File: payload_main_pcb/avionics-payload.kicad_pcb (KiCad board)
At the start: 2 copper layers, 80 x 80 mm, 27 parts, among them J1 Micro_SD_Card, J2 Conn_Coaxial_x2, J3 Screw_Terminal_01x02, SW1 SW_Push, SW2 SW_Push, SW3 SW_Push, U2 Teensy4.0, U3 RFM96W-433S2, U4 LT1129-3.3_SOT223, U5 ublox_SAM-M8Q, U6 MS5607-02BA, U7 ADIS16470AMLZ

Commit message: Lots of stuff
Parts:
- removed the J2 at (44.5, 44.5)
- removed the R1 at (51.0, 84.4)
- removed the Ref** at (69.8, 75.6)
- added C2: 100nF, Capacitor_SMD:C_1206_3216Metric_Pad1.42x1.75mm_HandSolder, F.Cu at (52.7, 63.5)
- added C5: 100nF, Capacitor_SMD:C_1206_3216Metric_Pad1.42x1.75mm_HandSolder, F.Cu at (103.5, 95.2)
- added C6: 100nF, Capacitor_SMD:C_1206_3216Metric_Pad1.42x1.75mm_HandSolder, F.Cu at (87.0, 43.0)
- added J1: USB_C_Receptacle_USB2.0, Connector_USB:USB_C_Receptacle_GCT_USB4085, F.Cu at (76.8, 49.5)
- added J3: Conn_Coaxial, Connector_Coaxial:SMA_Amphenol_132291_Vertical, F.Cu at (63.2, 45.0)
- added R10: 51, Resistor_SMD:R_1206_3216Metric_Pad1.42x1.75mm_HandSolder, F.Cu at (101.4, 72.4)
- added R11: 10, Resistor_SMD:R_1206_3216Metric_Pad1.42x1.75mm_HandSolder, F.Cu at (101.4, 69.7)
- added R5: 51, Resistor_SMD:R_1206_3216Metric_Pad1.42x1.75mm_HandSolder, F.Cu at (101.3, 61.0)
- added R6: 10, Resistor_SMD:R_1206_3216Metric_Pad1.42x1.75mm_HandSolder, F.Cu at (101.3, 58.3)
- added R8: 51, Resistor_SMD:R_1206_3216Metric_Pad1.42x1.75mm_HandSolder, F.Cu at (101.3, 66.5)
- added R9: 10, Resistor_SMD:R_1206_3216Metric_Pad1.42x1.75mm_HandSolder, F.Cu at (101.3, 64.0)
- added REF**: MountingHole_3.2mm_M3_Pad_Via, MountingHole:MountingHole_3.2mm_M3_Pad_Via, F.Cu at (54.6, 44.5)
- added REF**: MountingHole_3.2mm_M3_Pad_Via, MountingHole:MountingHole_3.2mm_M3_Pad_Via, F.Cu at (54.6, 115.6)
- added REF**: MountingHole_3.2mm_M3_Pad_Via, MountingHole:MountingHole_3.2mm_M3_Pad_Via, F.Cu at (115.6, 44.5)
- added REF**: MountingHole_3.2mm_M3_Pad_Via, MountingHole:MountingHole_3.2mm_M3_Pad_Via, F.Cu at (115.6, 115.6)
- added Ref**: Val**, footprints:logo, F.Cu at (36.3, 114.3)
- added U3: 74LS14, Package_DIP:DIP-14_W7.62mm_SMDSocket_SmallPads, F.Cu at (97.8, 45.7)
- D1, D2, D3, D4: value LED -> LED_RGBA; footprint LED_SMD:LED_1206_3216Metric_Pad1.42x1.75mm_HandSolder -> LED_SMD:LED_Avago_PLCC4_3.2x2.8mm_CW
- R2: value 220 -> R; footprint Resistor_SMD:R_0805_2012Metric_Pad1.15x1.40mm_HandSolder -> Resistor_SMD:R_1206_3216Metric_Pad1.42x1.75mm_HandSolder
- R3: value 220 -> 51; footprint Resistor_SMD:R_0805_2012Metric_Pad1.15x1.40mm_HandSolder -> Resistor_SMD:R_1206_3216Metric_Pad1.42x1.75mm_HandSolder
- R4: value 220 -> 10; footprint Resistor_SMD:R_0805_2012Metric_Pad1.15x1.40mm_HandSolder -> Resistor_SMD:R_1206_3216Metric_Pad1.42x1.75mm_HandSolder
- moved C4 79.5 mm to (67.1, 115.6), turned to 0 degrees
- moved J4 76.6 mm to (99.1, 116.2)
- moved D1 75.9 mm to (116.2, 53.2)
- moved D2 75.0 mm to (116.2, 59.1)
- moved U6 72.9 mm to (67.9, 112.4), turned to 90 degrees
- moved D4 72.8 mm to (116.3, 70.5)
- moved R3 66.8 mm to (101.3, 55.1), turned to 180 degrees
- moved D3 66.6 mm to (116.2, 64.8)
- moved R4 61.2 mm to (101.3, 52.5), turned to 180 degrees
- moved C3 56.3 mm to (106.7, 114.9), turned to 0 degrees
- moved R12 51.6 mm to (75.2, 113.8), turned to 90 degrees
- moved SW1 50.8 mm to (59.7, 106.7), turned to 180 degrees
- moved R7 49.4 mm to (75.6, 58.4), turned to 90 degrees
- moved R1 47.7 mm to (74.9, 101.4), turned to 270 degrees
- moved J2 47.4 mm to (87.0, 65.2), turned to 0 degrees
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- renumbered C10 to C3, C9 to C4, J1 to J2, J3 to J4, R5 to R1, R7 to R12, R6 to R7, SW3 to SW1, SW1 to SW2, SW2 to SW3, U7 to U1, U3 to U4, U4 to U5, U5 to U7
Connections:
- D1 pad 2: SystemStatus -> Net-(D1-Pad2)
- D2 pad 2: SensorStatus -> Net-(D2-Pad2)
- D3 pad 2: TransmitterStatus -> Net-(D3-Pad2)
- D4 pad 2: GPSStatus -> Net-(D4-Pad2)
- R2 pad 1: GND -> +3V3
- R2 pad 2: Net-(D2-Pad1) -> Net-(J1-PadA5)
- R3 pad 1: GND -> Net-(D1-Pad1)
- R3 pad 2: Net-(D3-Pad1) -> SystemStatus
- R4 pad 1: GND -> Net-(D1-Pad2)
- R4 pad 2: Net-(D4-Pad1) -> Net-(R4-Pad2)
- U2 pad 10: TX1 -> IMU_DR
- U2 pad 23: Net-(U2-Pad23) -> RX1
- U2 pad 24: Net-(U2-Pad24) -> TX1
- U2 pad 27: Net-(U2-Pad27) -> GPSStatus
- U2 pad 28: IMU_DR -> TransmitterStatus
- U2 pad 29: Net-(U2-Pad29) -> SensorStatus
- U2 pad 30: Net-(U2-Pad30) -> SystemStatus
- U2 pad 34: Net-(U2-Pad34) -> V_USB
- U2 pad 4: GPSStatus -> Net-(U2-Pad4)
- U2 pad 5: SensorStatus -> Net-(U2-Pad5)
- U2 pad 53: Net-(U2-Pad53) -> USB_D-
- U2 pad 54: Net-(U2-Pad54) -> USB_D+
- U2 pad 6: TransmitterStatus -> Net-(U2-Pad6)
- U2 pad 7: SystemStatus -> Net-(U2-Pad7)
- U2 pad 9: RX1 -> Net-(U2-Pad9)
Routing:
- net GND: track 408.1 -> 0.00 mm, vias 2 -> 0
- net +3V3: track 202.1 -> 251.5 mm, vias 0 -> 6
- net V_USB: track 0.00 -> 47.8 mm, vias 0 -> 1
- net USB_D-: track 0.00 -> 37.2 mm, vias 0 -> 1
- net USB_D+: track 0.00 -> 35.8 mm, vias 0 -> 1
- net MOSI2: track 17.8 -> 51.1 mm, vias 0 -> 1
- net MISO2: track 46.8 -> 18.0 mm
- net SCK2: track 23.9 -> 51.7 mm, vias 0 -> 1
- net CS2: track 56.8 -> 29.9 mm, vias 1 -> 0
- net Net-(J1-PadA5): track 0.00 -> 25.9 mm
- net Net-(R11-Pad2): track 0.00 -> 24.0 mm, vias 0 -> 2
- net Net-(R6-Pad2): track 0.00 -> 20.3 mm, vias 0 -> 2
- net Net-(D1-Pad1): track 32.3 -> 13.0 mm
- net Net-(R9-Pad2): track 0.00 -> 16.7 mm, vias 0 -> 2
- net Net-(SW1-Pad2): track 0.00 -> 16.4 mm
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- added copper zone on F.Cu, net GND
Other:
- board size 80 x 80 mm -> 69.8 x 80 mm
- board text added: "Designed for SOAR's Asterion"
- board text added: "GPS"
- board text added: "GPS Reset"
- board text added: "IMU Reset"
- board text added: "Sensors"
- board text added: "System"
- board text added: "Transmitter"
- board text added: "Transmitter Reset"
- board text removed: "GPS Status"
- board text removed: "Sensors Status"
- board text removed: "System Status"
- board text removed: "Transmitter Status"

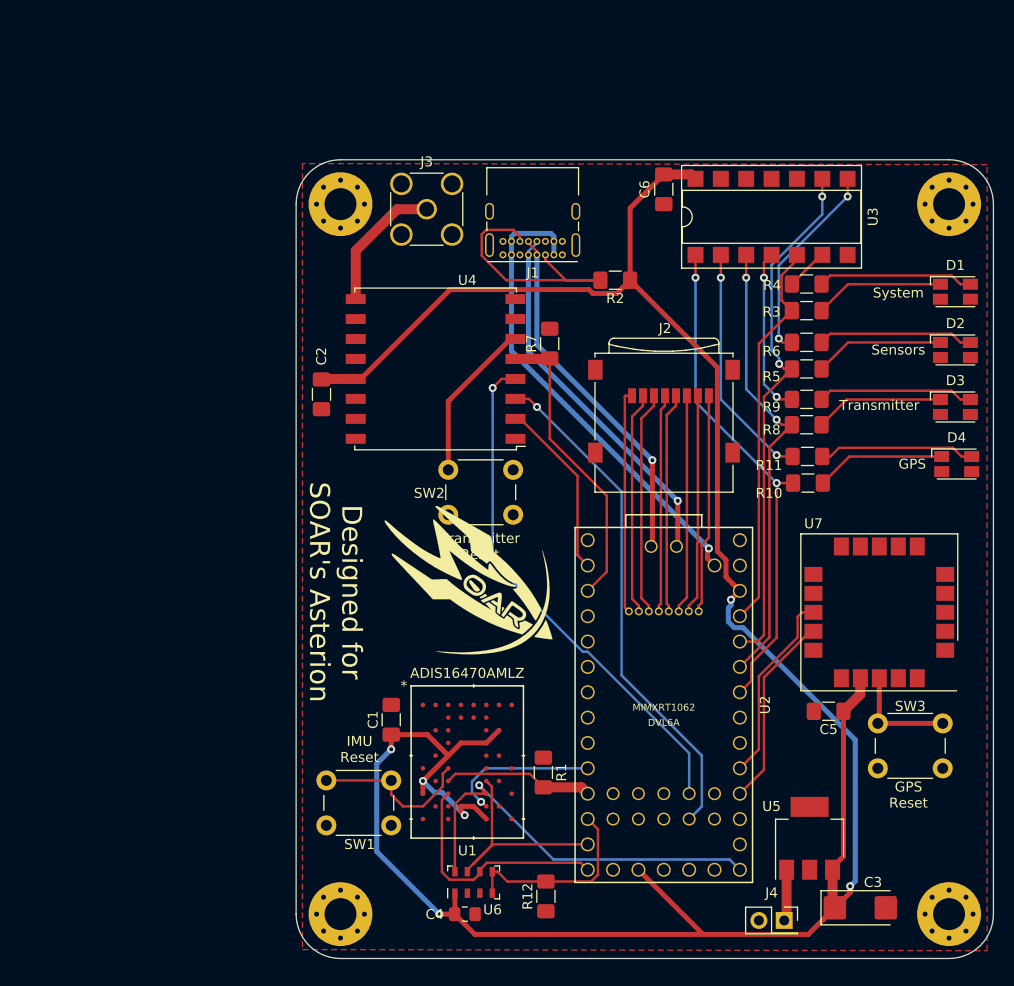
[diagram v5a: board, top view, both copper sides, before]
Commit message: Changed buttons and added bottom plane
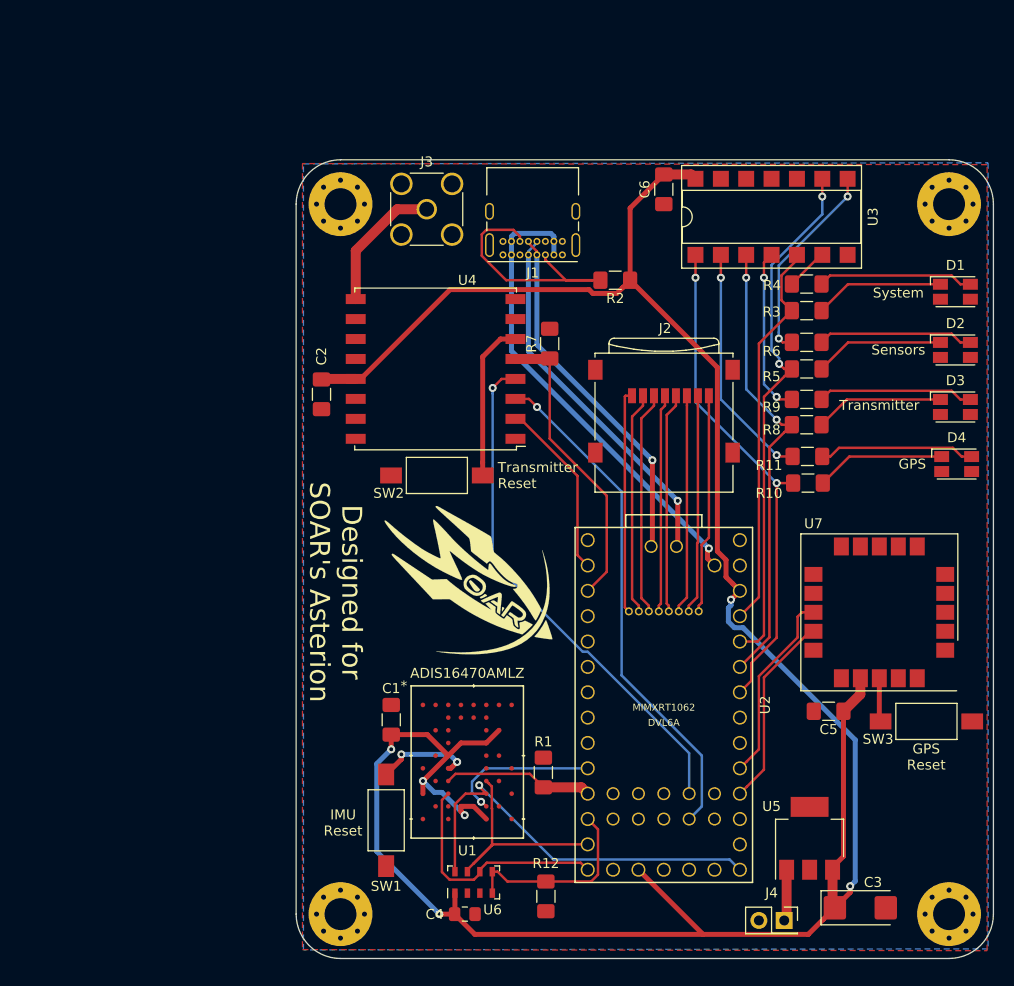
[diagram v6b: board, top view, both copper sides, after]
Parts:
- SW1, SW2, SW3: footprint Button_Switch_THT:SW_PUSH_6mm -> Button_Switch_SMD:SW_SPST_FSMSM
- moved SW2 8.60 mm to (64.3, 71.6), turned to 0 degrees
- moved SW3 4.97 mm to (113.3, 96.3)
- moved SW1 0.72 mm to (59.2, 106.2), turned to 90 degrees
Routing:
- net Net-(SW1-Pad2): track 16.4 -> 9.70 mm, vias 0 -> 2
- net Net-(SW3-Pad2): track 11.1 -> 4.38 mm
- added copper zone on B.Cu, net GND

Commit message: PCB REV A
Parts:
- removed the REF** at (54.6, 44.5)
- removed the REF** at (54.6, 115.6)
- removed the REF** at (115.6, 44.5)
- removed the REF** at (115.6, 115.6)
- added BT1: Battery_Cell, Battery:BatteryHolder_Keystone_1060_1x2032, B.Cu at (48.5, 69.3)
- added BZ1: Buzzer, Buzzer_Beeper:Buzzer_CUI_CPT-9019S-SMT, F.Cu at (70.5, 40.0)
- added C7: 100nF, Capacitor_SMD:C_1206_3216Metric_Pad1.42x1.75mm_HandSolder, F.Cu at (107.2, 78.7)
- added C8: 100nF, Capacitor_SMD:C_1206_3216Metric_Pad1.42x1.75mm_HandSolder, F.Cu at (107.2, 73.5)
- added C9: 100nF, Capacitor_SMD:C_1206_3216Metric_Pad1.42x1.75mm_HandSolder, F.Cu at (59.7, 70.8)
- added F1: Polyfuse, Fuse:Fuse_1812_4532Metric_Pad1.30x3.40mm_HandSolder, F.Cu at (82.5, 105.0)
- added J5: Conn_01x08, Connector_PinSocket_2.54mm:PinSocket_1x08_P2.54mm_Vertical, F.Cu at (41.0, 97.8)
- added R13: 11k, Resistor_SMD:R_1206_3216Metric_Pad1.42x1.75mm_HandSolder, F.Cu at (93.6, 91.8)
- added R14: 10M, Resistor_SMD:R_1206_3216Metric_Pad1.42x1.75mm_HandSolder, F.Cu at (61.0, 79.3)
- added R15: 3.3M, Resistor_SMD:R_1206_3216Metric_Pad1.42x1.75mm_HandSolder, F.Cu at (59.7, 74.8)
- added REF**: MountingHole_3.2mm_M3_Pad, MountingHole:MountingHole_3.2mm_M3_Pad, F.Cu at (104.0, 47.0)
- added REF**: MountingHole_3.2mm_M3_Pad, MountingHole:MountingHole_3.2mm_M3_Pad, F.Cu at (104.0, 93.0)
- added REF**: MountingHole_3.2mm_M3_Pad, MountingHole:MountingHole_3.2mm_M3_Pad, F.Cu at (36.0, 93.0)
- added REF**: MountingHole_3.2mm_M3_Pad, MountingHole:MountingHole_3.2mm_M3_Pad, F.Cu at (36.0, 47.0)
- added SW4: SW_SPST, Button_Switch_SMD:SW_DIP_SPSTx01_Slide_6.7x4.1mm_W6.73mm_P2.54mm_LowProfile_JPin, F.Cu at (74.1, 104.9)
- added TP1: TestPoint, Connector_Pin:Pin_D1.0mm_L10.0mm, F.Cu at (103.1, 68.7)
- added TP2: TestPoint, TestPoint:TestPoint_Loop_D2.50mm_Drill1.0mm, F.Cu at (58.5, 64.0)
- added TP3: TestPoint, TestPoint:TestPoint_Loop_D2.50mm_Drill1.0mm, F.Cu at (55.8, 66.5)
- added TP4: TestPoint, TestPoint:TestPoint_Loop_D2.50mm_Drill1.0mm, F.Cu at (61.2, 61.5)
- C3: footprint Capacitor_Tantalum_SMD:CP_EIA-6032-15_Kemet-U_Pad2.25x2.35mm_HandSolder -> Capacitor_SMD:CP_Elec_4x5.4
- C4: footprint Capacitor_SMD:C_0805_2012Metric_Pad1.15x1.40mm_HandSolder -> Capacitor_SMD:C_1206_3216Metric_Pad1.42x1.75mm_HandSolder
- moved J4 34.1 mm to (66.9, 104.9)
- moved Ref** 23.8 mm to (14.5, 104.8)
- moved U5 21.8 mm to (86.6, 92.2)
- moved R2 21.5 mm to (62.5, 43.3), turned to 90 degrees
- moved C3 21.3 mm to (95.5, 96.8)
- moved R1 18.0 mm to (59.9, 91.4)
- moved C1 18.0 mm to (44.7, 86.1)
- moved R12 18.0 mm to (60.2, 103.8)
- moved SW1 18.0 mm to (44.2, 96.2)
- moved SW2 18.0 mm to (49.3, 61.6)
- moved U1 18.0 mm to (52.3, 90.3)
- moved U2 18.0 mm to (72.0, 84.6)
- moved U7 18.0 mm to (93.6, 75.3)
- moved J1 18.0 mm to (61.8, 39.5)
- moved U6 18.0 mm to (52.9, 102.4)
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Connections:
- U2 pad 21: Net-(U2-Pad21) -> GPS_EXTINT
- U2 pad 22: Net-(U2-Pad22) -> BATT_SENSE
- U2 pad 25: Net-(U2-Pad25) -> SDA
- U2 pad 26: Net-(U2-Pad26) -> SCL
- U2 pad 4: Net-(U2-Pad4) -> BUZZER
- U2 pad 9: Net-(U2-Pad9) -> INT
- U5 pad 1: +BATT -> Net-(F1-Pad1)
- U7 pad 19: Net-(U7-Pad19) -> GPS_EXTINT
- U7 pad 2: Net-(U7-Pad2) -> +3V3
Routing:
- net Net-(BT1-Pad1): track 0.00 -> 123.5 mm, vias 0 -> 1
- net +3V3: track 251.5 -> 345.0 mm, vias 6 -> 9
- net SCL: track 0.00 -> 58.8 mm, vias 0 -> 2
- net SDA: track 0.00 -> 52.7 mm, vias 0 -> 2
- net +BATT: track 5.18 -> 55.9 mm
- net Net-(F1-Pad1): track 0.00 -> 43.8 mm
- net BATT_SENSE: track 0.00 -> 37.8 mm
- net BUZZER: track 0.00 -> 34.3 mm
- net GPS_EXTINT: track 0.00 -> 30.0 mm, vias 0 -> 1
- net INT: track 0.00 -> 26.9 mm, vias 0 -> 1
- net Net-(TP1-Pad1): track 0.00 -> 13.9 mm
- net GND: track 0.00 -> 10.2 mm, vias 0 -> 180
- net Net-(D1-Pad2): track 15.6 -> 24.5 mm
- net SensorStatus: track 52.9 -> 60.9 mm
- net Net-(D2-Pad2): track 15.6 -> 23.6 mm
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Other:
- board size 69.8 x 80 mm -> 78 x 78 mm
- board text added: "+"
- board text added: "-"
- board text added: "MAX 12V"
- board text added: "ONLY ON"
- board text added: "Off/On"
- board text added: "REV A"

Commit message: REV B
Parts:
- removed C8, C9: 100nF, Capacitor_SMD:C_1206_3216Metric_Pad1.42x1.75mm_HandSolder
- removed D1, D2, D3, D4: LED_RGBA, LED_SMD:LED_Avago_PLCC4_3.2x2.8mm_CW
- removed F1: Polyfuse, Fuse:Fuse_1812_4532Metric_Pad1.30x3.40mm_HandSolder
- removed the J5 at (41.0, 97.8)
- removed R10, R5, R8: 51, Resistor_SMD:R_1206_3216Metric_Pad1.42x1.75mm_HandSolder
- removed R11, R6, R9: 10, Resistor_SMD:R_1206_3216Metric_Pad1.42x1.75mm_HandSolder
- removed R12, R7: 10k, Resistor_SMD:R_1206_3216Metric_Pad1.42x1.75mm_HandSolder
- removed R13: 11k, Resistor_SMD:R_1206_3216Metric_Pad1.42x1.75mm_HandSolder
- removed R14: 10M, Resistor_SMD:R_1206_3216Metric_Pad1.42x1.75mm_HandSolder
- removed R15: 3.3M, Resistor_SMD:R_1206_3216Metric_Pad1.42x1.75mm_HandSolder
- removed SW4: SW_SPST, Button_Switch_SMD:SW_DIP_SPSTx01_Slide_6.7x4.1mm_W6.73mm_P2.54mm_LowProfile_JPin
- removed the U2 at (72.0, 84.6)
- removed U5: LT1129-3.3_SOT223, Package_TO_SOT_SMD:SOT-223-3_TabPin2
- removed U7: ublox_SAM-M8Q, RF_GPS:ublox_SAM-M8Q
- added J1: Conn_02x14_Counter_Clockwise, Connector_PinSocket_2.54mm:PinSocket_2x14_P2.54mm_Vertical, F.Cu at (75.5, 66.1)
- added J3: Conn_02x08_Odd_Even, Connector_PinHeader_2.00mm:PinHeader_2x08_P2.00mm_Vertical_SMD, F.Cu at (85.8, 73.0)
- added J6: Micro_SD_Card, Connector_Card:microSD_HC_Wuerth_693072010801, F.Cu at (40.0, 59.2)
- added Ref**: Val**, footprints:drawing, B.Cu at (45.2, 105.0)
- C3: value 3.3uF -> 100nF; footprint Capacitor_SMD:CP_Elec_4x5.4 -> Capacitor_SMD:C_1206_3216Metric_Pad1.42x1.75mm_HandSolder
- C7: value 100nF -> 3.3uF; footprint Capacitor_SMD:C_1206_3216Metric_Pad1.42x1.75mm_HandSolder -> Capacitor_SMD:CP_Elec_4x3.9
- J2: value Micro_SD_Card -> Conn_01x02; footprint Connector_Card:microSD_HC_Wuerth_693072010801 -> TerminalBlock:TerminalBlock_bornier-2_P5.08mm
- J4: value Screw_Terminal_01x02 -> Conn_02x14_Counter_Clockwise; footprint Connector_PinSocket_2.54mm:PinSocket_2x01_P2.54mm_Vertical -> Connector_PinSocket_2.54mm:PinSocket_2x14_P2.54mm_Vertical
- R2: value R -> 10k
- R3: value 51 -> 11k
- R4: value 10 -> 10k
- TP1: footprint Connector_Pin:Pin_D1.0mm_L10.0mm -> TestPoint:TestPoint_Loop_D2.50mm_Drill1.0mm
- TP4: footprint TestPoint:TestPoint_Loop_D2.50mm_Drill1.0mm -> Connector_Pin:Pin_D1.0mm_L10.0mm
- U1: value ADIS16470AMLZ -> RFM95W-915S2; footprint footprints:ADIS16470AMLZ -> RF_Module:HOPERF_RFM9XW_SMD
- U3: value 74LS14 -> ublox_SAM-M8Q; footprint Package_DIP:DIP-14_W7.62mm_SMDSocket_SmallPads -> RF_GPS:ublox_SAM-M8Q
- U4: value RFM96W-433S2 -> LT1129-3.3_SOT223; footprint RF_Module:HOPERF_RFM9XW_SMD -> Package_TO_SOT_SMD:SOT-223-3_TabPin2
- moved Ref** 76.6 mm to (90.8, 97.5), turned to 0 degrees
- moved U3 61.7 mm to (57.8, 91.5), turned to 180 degrees
- moved U2 61.3 mm to (103.0, 67.0)
- moved C4 58.8 mm to (100.5, 71.5), turned to 270 degrees
- moved U4 58.5 mm to (88.0, 96.0)
- moved J5 57.4 mm to (103.5, 79.0), turned to 90 degrees
- moved C6 55.2 mm to (68.5, 89.0), turned to 180 degrees
- moved TP3 53.8 mm to (95.5, 102.8), turned to 0 degrees
- moved R3 51.9 mm to (69.0, 96.5), turned to 90 degrees
- moved U1 51.7 mm to (63.0, 39.8), turned to 180 degrees
- moved J2 49.7 mm to (84.2, 104.5)
- moved J4 47.0 mm to (93.3, 66.1), turned to 180 degrees
- moved SW1 46.9 mm to (88.2, 80.0), turned to 0 degrees
- moved TP1 43.3 mm to (78.8, 104.5)
- moved C3 41.6 mm to (54.2, 101.5), turned to 180 degrees
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- renumbered J1 to J5, J3 to J7, U6 to U2
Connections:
- C6 pad 1: +3V3 -> GND
- C6 pad 2: GND -> Net-(BT1-Pad1)
- J2 pad 1: SD_DAT2 -> GND
- J2 pad 2: SD_DAT3 -> +BATT
- J4 pad 1: +BATT -> /vin
- J5 pad A5: Net-(J1-PadA5) -> Net-(J5-PadA5)
- J5 pad B5: Net-(J1-PadA5) -> Net-(J5-PadB5)
- J7 pad 1: Net-(J3-Pad1) -> Net-(J7-Pad1)
- R2 pad 1: +3V3 -> CS2
- R2 pad 2: Net-(J1-PadA5) -> GND
- R3 pad 1: Net-(D1-Pad1) -> Net-(R3-Pad1)
- R3 pad 2: SystemStatus -> +3V3
- R4 pad 1: Net-(D1-Pad2) -> GND
- R4 pad 2: Net-(R4-Pad2) -> CS1:1
- SW1 pad 2: Net-(SW1-Pad2) -> Net-(J3-Pad1)
- SW3 pad 2: Net-(R13-Pad1) -> Net-(R3-Pad1)
- TP1 pad 1: Net-(TP1-Pad1) -> GND
- TP2 pad 1: GND -> +3V3
- TP3 pad 1: +3V3 -> +BATT
- TP4 pad 1: +BATT -> Net-(TP4-Pad1)
- U3 pad 1: GPSStatus -> GND
- U3 pad 10: (no net) -> GND
- U3 pad 11: (no net) -> GND
- U3 pad 12: (no net) -> Net-(U3-Pad12)
- U3 pad 13: (no net) -> TX1
- U3 pad 14: +3V3 -> RX1
- U3 pad 2: Net-(R11-Pad2) -> +3V3
- U3 pad 3: TransmitterStatus -> Net-(BT1-Pad1)
- U3 pad 4: Net-(R9-Pad2) -> GND
- U3 pad 5: SystemStatus -> GND
- U3 pad 6: Net-(R4-Pad2) -> GND
- U3 pad 7: GND -> Net-(U3-Pad7)
- U3 pad 8: Net-(R6-Pad2) -> Net-(TP4-Pad1)
- U3 pad 9: SensorStatus -> Net-(U3-Pad9)
- U4 pad 1: GND -> +BATT
- U4 pad 2: MISO2 -> GND
- U4 pad 3: MOSI2 -> +3V3
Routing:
- net +3V3: track 345.0 -> 186.5 mm, vias 9 -> 3
- net Net-(BT1-Pad1): track 123.5 -> 29.7 mm
- net SensorStatus: track 60.9 -> 0.00 mm, vias 2 -> 0
- net SCL: track 58.8 -> 0.00 mm, vias 2 -> 0
- net SDA: track 52.7 -> 0.00 mm, vias 2 -> 0
- net RX1: track 19.5 -> 68.5 mm, vias 0 -> 1
- net GPSStatus: track 48.6 -> 0.00 mm, vias 2 -> 0
- net TX1: track 19.4 -> 67.3 mm, vias 0 -> 1
- net Net-(F1-Pad1): track 43.8 -> 0.00 mm
- net TransmitterStatus: track 43.6 -> 0.00 mm, vias 2 -> 0
- net GPS_EXTINT: track 30.0 -> 73.5 mm, vias 1 -> 3
- net +BATT: track 55.9 -> 14.1 mm
- net SystemStatus: track 41.1 -> 0.00 mm, vias 2 -> 0
- net BATT_SENSE: track 37.8 -> 0.00 mm
- net CS1:1: track 19.8 -> 52.1 mm, vias 2 -> 3
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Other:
- board text added: "Designed for Asterion"
- board text added: "REV B"
- board text removed: "+"
- board text removed: "-"
- board text removed: "Designed for SOAR's Asterion"
- board text removed: "GPS"
- board text removed: "GPS Reset"
- board text removed: "IMU Reset"
- board text removed: "MAX 12V"
- board text removed: "ONLY ON"
- board text removed: "Off/On"
- board text removed: "REV A"
- board text removed: "Sensors"
- board text removed: "System"
- board text removed: "Transmitter"
- board text removed: "Transmitter Reset"
